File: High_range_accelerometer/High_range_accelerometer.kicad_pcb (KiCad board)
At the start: 2 copper layers, 30 x 70 mm, 55 parts, among them J1 USB_B_Micro, P1 KRC_PSoCWriter, U1 KRC_Conn_CAN, U2 LT1965xDD-3.3, U3 LT1761-5, U4 NCV7342, U5 CY8C5868LTI-LP039, U6 H3LIS331DLTR, U7 W25N01GVxxIG-IT, Y1 Crystal_kHz, Y2 Crystal_MHz

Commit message: とりあえずできた
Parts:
- removed C21, C22: 9pF, Capacitor_SMD:C_0201_0603Metric
- removed Y1: Crystal_kHz, KUTKiCad_footprint:Crystal_SeikoEpson_FC-135
- added C15: 0.1uF, Capacitor_SMD:C_0402_1005Metric, F.Cu at (99.8, 87.4)
- C10, C12, C13, C17, C20, C23, C24, C25, C27, C4, C7, C8, C9: footprint Capacitor_SMD:C_0201_0603Metric -> Capacitor_SMD:C_0402_1005Metric
- C11, C14, C16, C18, C19, C2: footprint Capacitor_SMD:C_0603_1608Metric -> Capacitor_SMD:C_0402_1005Metric
- J1: footprint Connector_USB:USB_Micro-B_Amphenol_10103594-0001LF_Horizontal -> KUTKiCad_footprint:Hirose_ZX_ZX62D-B-5P8
- R10, R11, R2, R3, R4, R5, R6, R7, R8, R9: footprint Resistor_SMD:R_0603_1608Metric -> Capacitor_SMD:C_0402_1005Metric
- U5: footprint Package_DFN_QFN:QFN-68-1EP_8x8mm_P0.4mm_EP5.2x5.2mm_ThermalVias -> KUTKiCad_footprint:Cypress_QFN-68_EP_8x8_Pitch0.4mm
- moved C26 33.6 mm to (117.4, 69.8), turned to 90 degrees
- moved U6 28.1 mm to (117.9, 73.6), turned to 270 degrees
- moved R8 26.4 mm to (113.3, 73.4)
- moved J1 23.7 mm to (94.7, 102.8), turned to 270 degrees
- moved C24 23.2 mm to (118.9, 70.6), turned to 90 degrees
- moved P1 15.6 mm to (95.4, 77.7)
- moved R1 13.6 mm to (116.2, 62.1), turned to 180 degrees
- moved R10 13.1 mm to (108.3, 101.7)
- moved R6 11.7 mm to (116.7, 64.1), turned to 180 degrees
- moved R7 11.3 mm to (116.7, 66.1), turned to 180 degrees
- moved R9 9.61 mm to (109.5, 101.7), turned to 90 degrees
- moved R11 8.22 mm to (107.1, 101.7), turned to 90 degrees
- moved R5 6.86 mm to (104.8, 101.7), turned to 90 degrees
- moved R4 6.25 mm to (106.0, 101.7), turned to 90 degrees
- moved C27 5.77 mm to (110.6, 101.7), turned to 90 degrees
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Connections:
- D2 pad 1: Net-(D2-Pad1) -> LED_G_1
- D3 pad 1: Net-(D3-Pad1) -> LED_G_2
- P1 pad 1: Net-(P1-Pad1) -> (no net)
- U3 pad 4: Net-(U3-Pad4) -> (no net)
- U5 pad 1: Net-(U5-Pad1) -> (no net)
- U5 pad 13: Net-(U5-Pad13) -> (no net)
- U5 pad 14: Net-(U5-Pad14) -> (no net)
- U5 pad 15: Net-(U5-Pad15) -> (no net)
- U5 pad 16: Net-(U5-Pad16) -> (no net)
- U5 pad 18: Net-(U5-Pad18) -> (no net)
- U5 pad 19: Net-(U5-Pad19) -> (no net)
- U5 pad 2: Net-(U5-Pad2) -> (no net)
- U5 pad 29: Net-(D2-Pad1) -> (no net)
- U5 pad 30: Net-(D3-Pad1) -> (no net)
- U5 pad 31: Net-(U5-Pad31) -> (no net)
- U5 pad 32: Net-(U5-Pad32) -> (no net)
- U5 pad 33: Net-(U5-Pad33) -> (no net)
- U5 pad 34: Net-(U5-Pad34) -> (no net)
- U5 pad 36: Net-(U5-Pad36) -> (no net)
- U5 pad 37: Net-(U5-Pad37) -> (no net)
- U5 pad 38: Sensor-CLK -> (no net)
- U5 pad 39: Sensor-MOSI -> (no net)
- U5 pad 40: Net-(C22-Pad1) -> (no net)
- U5 pad 41: Net-(C21-Pad1) -> (no net)
- U5 pad 47: Sensor-CS -> Sensor-CLK
- U5 pad 48: INT1 -> Sensor-MOSI
- U5 pad 49: INT2 -> Sensor-CS
- U5 pad 50: Net-(U5-Pad50) -> INT1
- U5 pad 51: Net-(U5-Pad51) -> INT2
- U5 pad 53: Net-(U5-Pad53) -> (no net)
- U5 pad 54: Net-(U5-Pad54) -> (no net)
- U5 pad 55: Net-(U5-Pad55) -> LED_G_1
- U5 pad 56: Net-(U5-Pad56) -> LED_G_2
- U5 pad 6: Net-(U5-Pad6) -> (no net)
- U5 pad 60: Net-(U5-Pad60) -> (no net)
- U5 pad 61: Net-(U5-Pad61) -> (no net)
- U5 pad 65: Net-(U5-Pad65) -> (no net)
- U5 pad 66: Net-(U5-Pad66) -> (no net)
- U5 pad 68: Net-(U5-Pad68) -> (no net)
- U6 pad 2: Net-(U6-Pad2) -> (no net)
- U6 pad 3: Net-(U6-Pad3) -> (no net)
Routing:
- net GND: track 28.1 -> 134.9 mm, vias 0 -> 101
- net +3V3: track 79.2 -> 141.3 mm, vias 3 -> 2
- net Flash-MOSI: track 0.00 -> 52.2 mm, vias 0 -> 2
- net Flash-CLK: track 0.00 -> 47.0 mm, vias 0 -> 2
- net Flash-~CS: track 0.00 -> 29.3 mm, vias 0 -> 2
- net Flash-MISO: track 0.00 -> 26.2 mm, vias 0 -> 2
- net LED_G_1: track 0.00 -> 22.5 mm, vias 0 -> 2
- net LED_G_2: track 0.00 -> 21.7 mm, vias 0 -> 2
- net Sensor-CLK: track 0.00 -> 20.3 mm, vias 0 -> 2
- net Sensor-MISO: track 0.00 -> 20.1 mm, vias 0 -> 4
- net Net-(R4-Pad2): track 0.00 -> 19.8 mm, vias 0 -> 2
- net Sensor-MOSI: track 0.00 -> 19.1 mm, vias 0 -> 2
- net Sensor-CS: track 0.00 -> 15.9 mm, vias 0 -> 2
- net SDATA: track 0.00 -> 15.0 mm, vias 0 -> 1
- net Net-(R5-Pad2): track 6.23 -> 21.0 mm, vias 0 -> 2
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- added copper zone on B.Cu, net GND
- added copper zone on F.Cu, net GND
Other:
- outline, holes or cut-outs redrawn

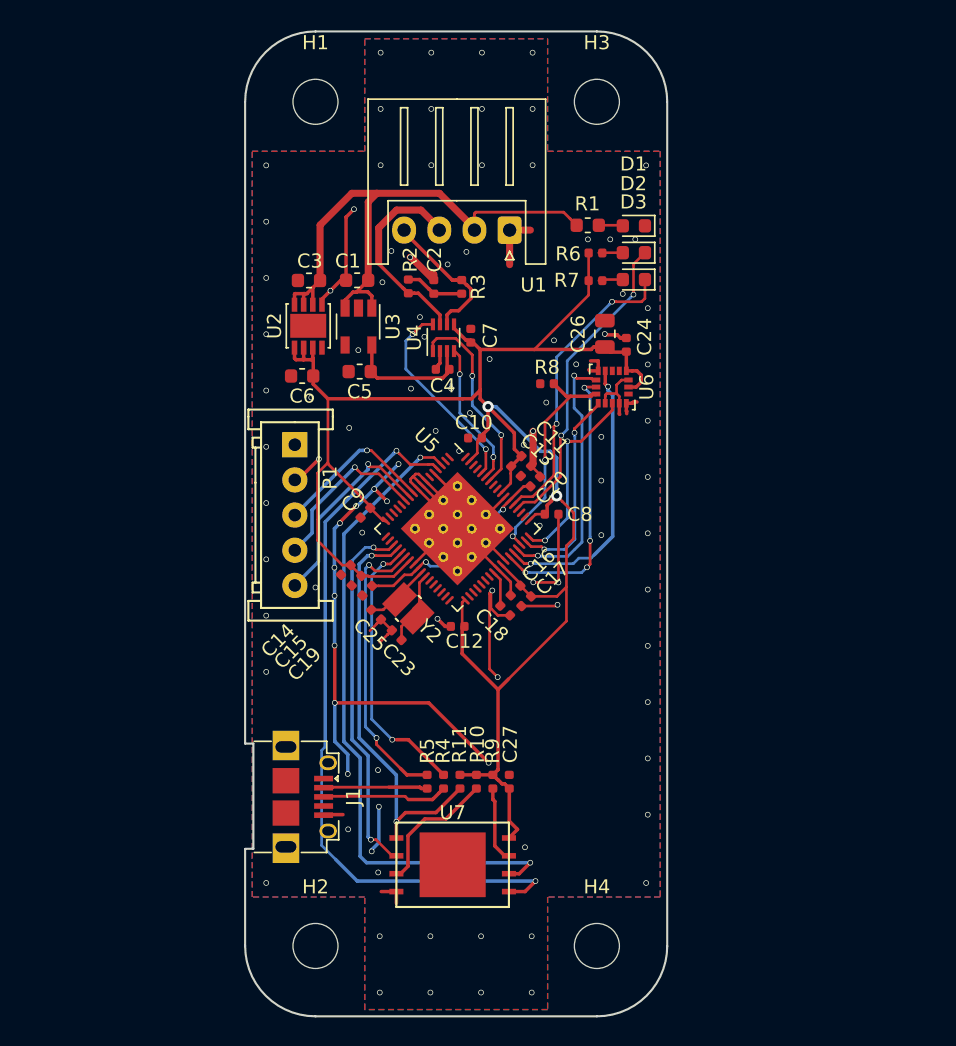
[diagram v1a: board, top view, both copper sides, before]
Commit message: change regulator
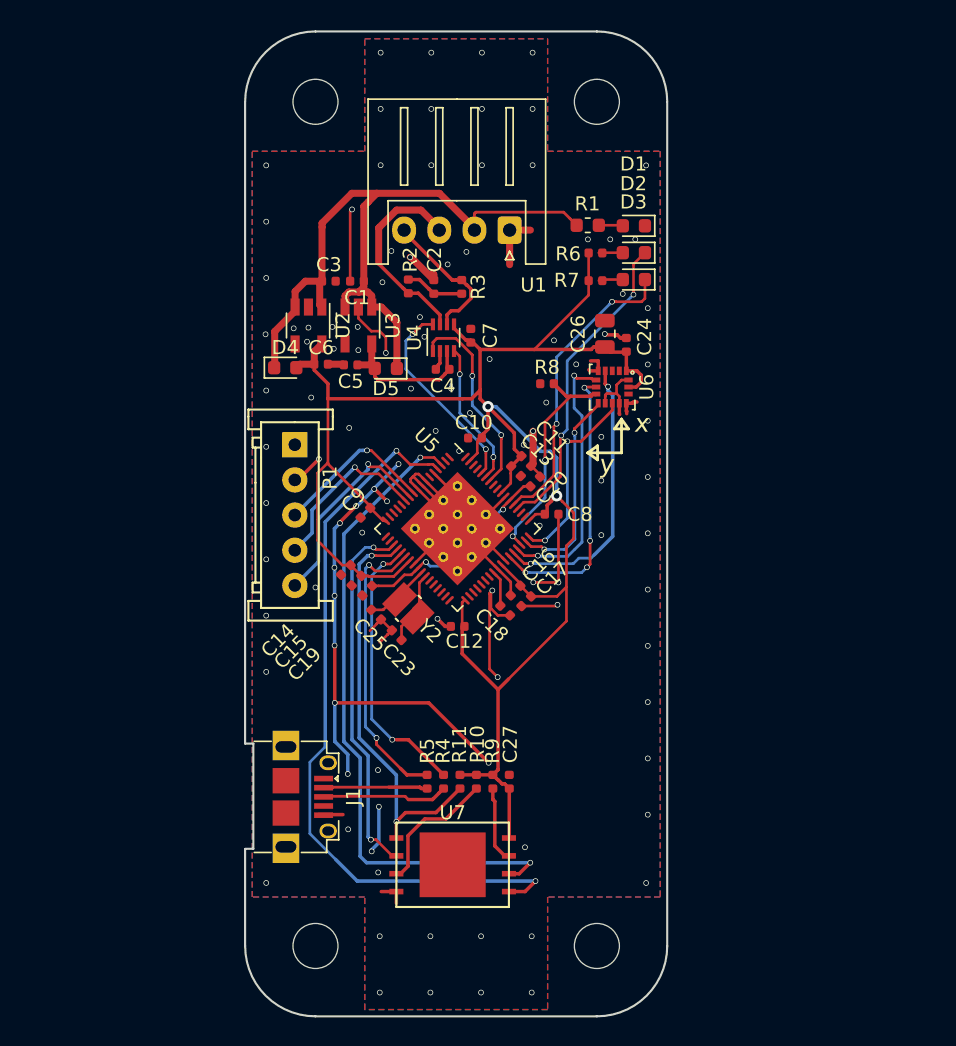
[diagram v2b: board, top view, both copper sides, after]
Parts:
- added D4: D_Schottky_Small, Diode_SMD:D_0603_1608Metric, F.Cu at (94.7, 72.2)
- added D5: D_Schottky_Small, Diode_SMD:D_0603_1608Metric, F.Cu at (101.8, 72.3)
- C1, C3, C5, C6: value 10uF -> 1uF; footprint Capacitor_SMD:C_0603_1608Metric -> Capacitor_SMD:C_0402_1005Metric
- U2: value LT1965xDD-3.3 -> NCP718ASN330T1G; footprint KUTKiCad_footprint:DFN-8-1EP_3x3mm_P0.65mm_EP1.7x2.56mm -> Package_TO_SOT_SMD:TSOT-23-5
- U3: value LT1761-5 -> NCP718ASN500T1G
- moved C6 1.59 mm to (97.2, 72.0), turned to 0 degrees
- moved C3 1.41 mm to (97.8, 66.1), turned to 0 degrees
- moved C5 0.80 mm to (99.3, 72.0)
- moved U3 0.07 mm to (99.9, 69.2)
- moved C1 0.06 mm to (99.8, 66.1)
- turned U2 to 270 degrees
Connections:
- J1 pad 1: Net-(J1-Pad1) -> (no net)
- J1 pad 4: Net-(J1-Pad4) -> (no net)
- U2 pad 1: +3V3 -> Net-(C1-Pad1)
- U2 pad 2: +3V3 -> GND
- U2 pad 3: +3V3 -> Net-(C1-Pad1)
- U2 pad 4: GND -> (no net)
- U2 pad 5: GND -> +3V3
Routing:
- net Net-(C1-Pad1): track 42.1 -> 52.9 mm
- net GND: track 134.9 -> 137.9 mm, vias 101 -> 107
- net +3V3: track 141.3 -> 139.6 mm
- net +5V: track 9.28 -> 10.8 mm
- net Flash-MOSI: track 52.2 -> 52.9 mm
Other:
- board text added: "CANH"
- board text added: "CANL"
- board text added: "Designed by ringo @Malus_Mill_"
- board text added: "GND"
- board text added: "VDD"
- board text added: "x"
- board text added: "y"

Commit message: add SVG and PDF and Gerber files
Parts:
- added G***: LOGO, my_footprint:Twitter_logo, B.Cu at (119.0, 95.4)
- added REF**: KiCad-Logo2_6mm_SilkScreen, Symbol:KiCad-Logo2_6mm_SilkScreen, B.Cu at (118.2, 64.0)
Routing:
- net GND: track 137.9 -> 134.4 mm, vias 107 -> 104
- net (no net): track 0.01 -> 3.48 mm, vias 0 -> 3
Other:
- board text added: "@Malus_Mill_"
- board text added: "Designed by ringo"
- board text added: "SCLK"
- board text added: "SDATA"
- board text added: "VBUS"
- board text added: "XRESS"
- board text removed: "Designed by ringo @Malus_Mill_"

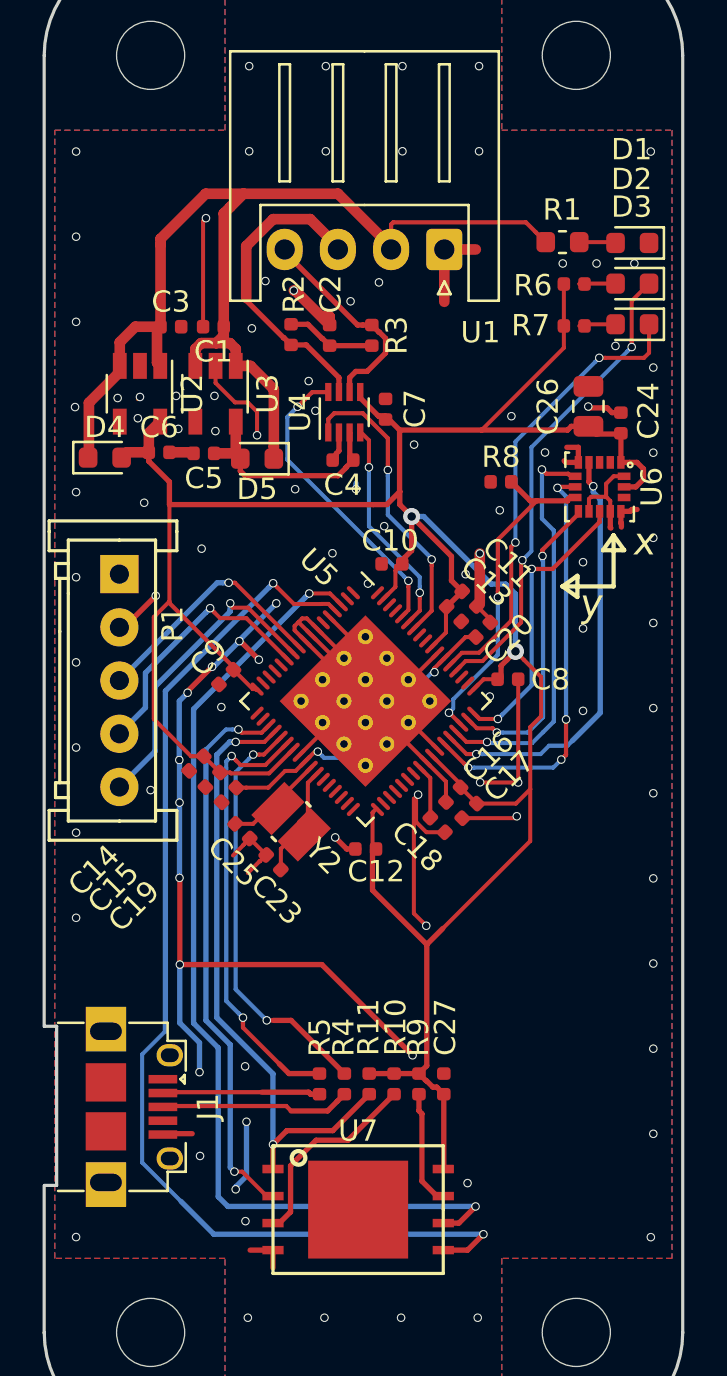
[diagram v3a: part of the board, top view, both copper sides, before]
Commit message: add sdCard
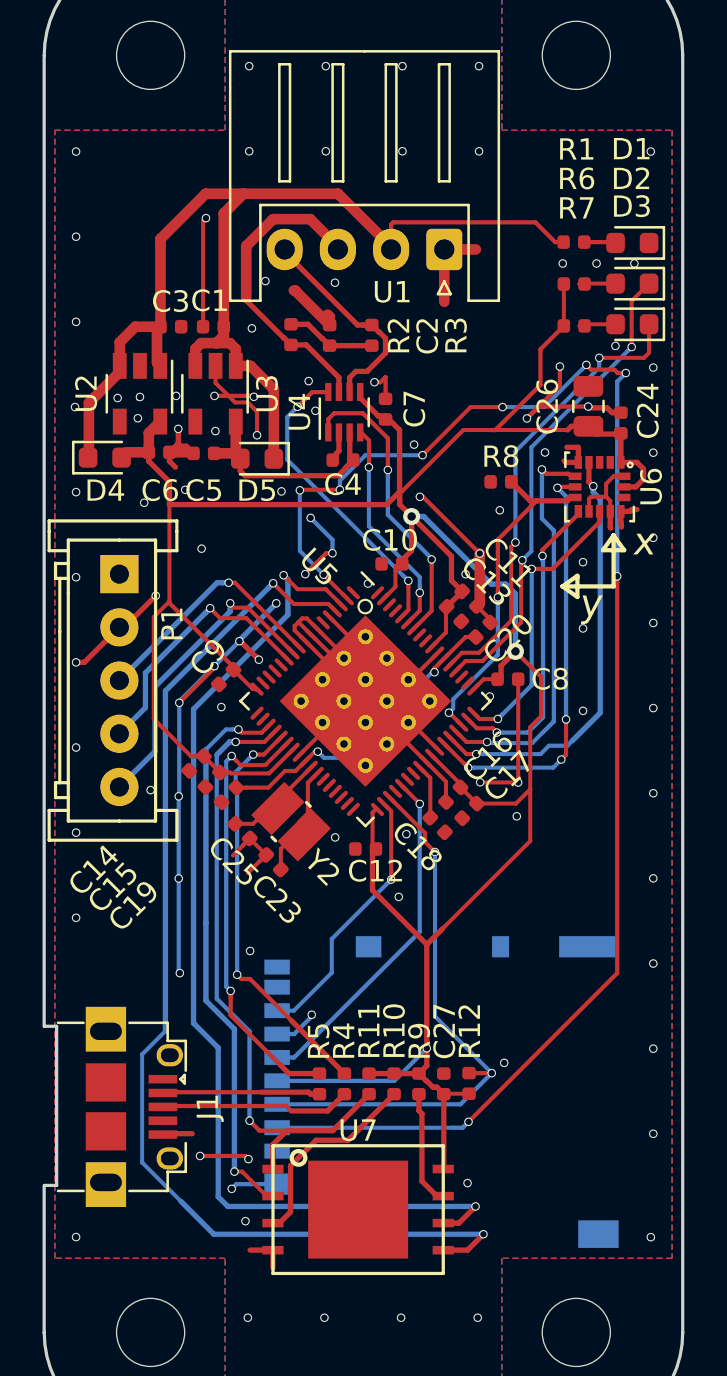
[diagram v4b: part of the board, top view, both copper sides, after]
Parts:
- added J2: Micro_SD_Card_Det_Hirose_DM3AT, Connector_Card:microSD_HC_Hirose_DM3AT-SF-PEJM5, B.Cu at (110.5, 102.1)
- added R12: 4.7kΩ, Resistor_SMD:R_0402_1005Metric, F.Cu at (111.8, 101.7)
- R1: footprint Resistor_SMD:R_0603_1608Metric -> Resistor_SMD:R_0402_1005Metric
- R10, R11, R2, R3, R4, R5, R6, R7, R8, R9: footprint Capacitor_SMD:C_0402_1005Metric -> Resistor_SMD:R_0402_1005Metric
- moved REF** 22.8 mm to (95.5, 64.6)
- moved G*** 13.6 mm to (115.6, 82.2)
- moved R1 0.54 mm to (116.7, 62.1)
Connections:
- U5 pad 2: (no net) -> microSD-~CS
- U5 pad 36: (no net) -> microSD-MISO
- U5 pad 37: (no net) -> microSD-MOSI
- U5 pad 39: (no net) -> microSD-CLK
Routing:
- net microSD-~CS: track 0.00 -> 71.5 mm, vias 0 -> 9
- net microSD-MOSI: track 0.00 -> 26.7 mm, vias 0 -> 2
- net microSD-CLK: track 0.00 -> 16.4 mm, vias 0 -> 1
- net microSD-MISO: track 0.00 -> 12.6 mm, vias 0 -> 1
- net +3V3: track 139.6 -> 149.6 mm, vias 2 -> 3
- net (no net): track 3.48 -> 0.01 mm, vias 3 -> 0
- net Flash-CLK: track 47.0 -> 49.1 mm
- net GND: track 134.4 -> 135.3 mm, vias 104 -> 109
- net Net-(C1-Pad1): track 52.9 -> 53.7 mm
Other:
- board text added: "rev. 1.2"
